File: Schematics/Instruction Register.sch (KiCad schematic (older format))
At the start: 44 parts, among them U46 74F157, U47 74F157, U48 74F574, U49 74F157, U50 74F157, U51 74F574

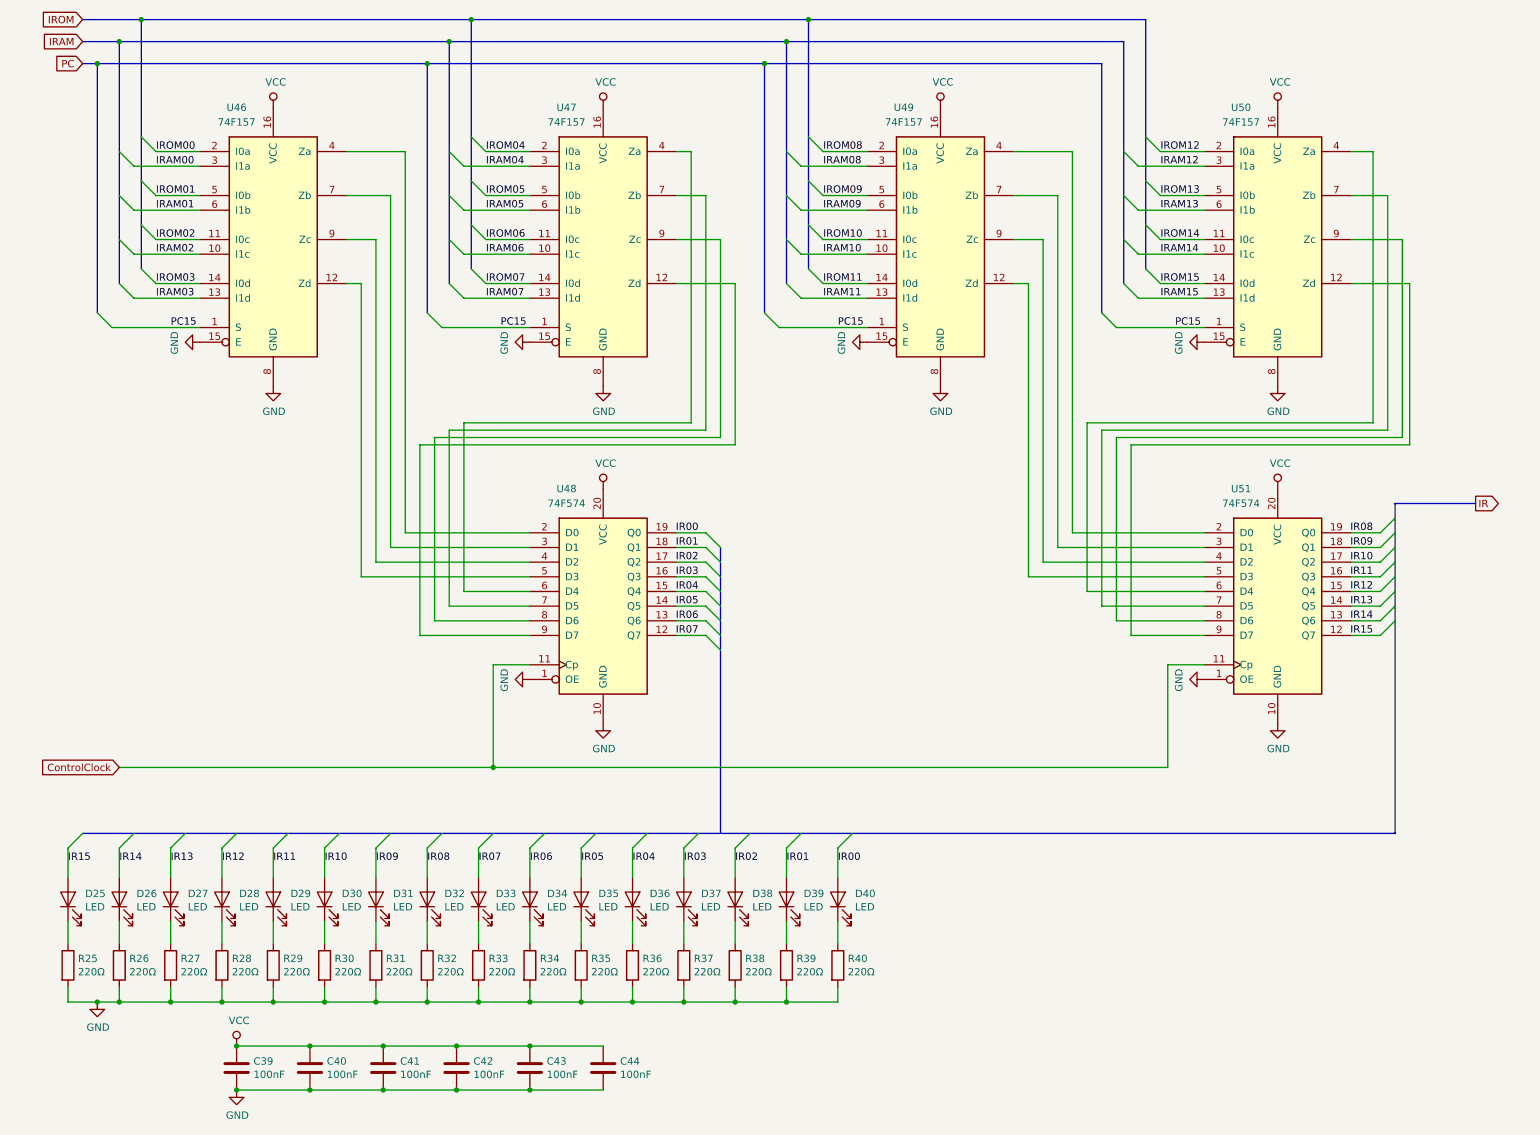
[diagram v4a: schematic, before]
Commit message: My buses were not named according the rules in the Eeschema manual.
Buses which connect to global labels must be named specially.
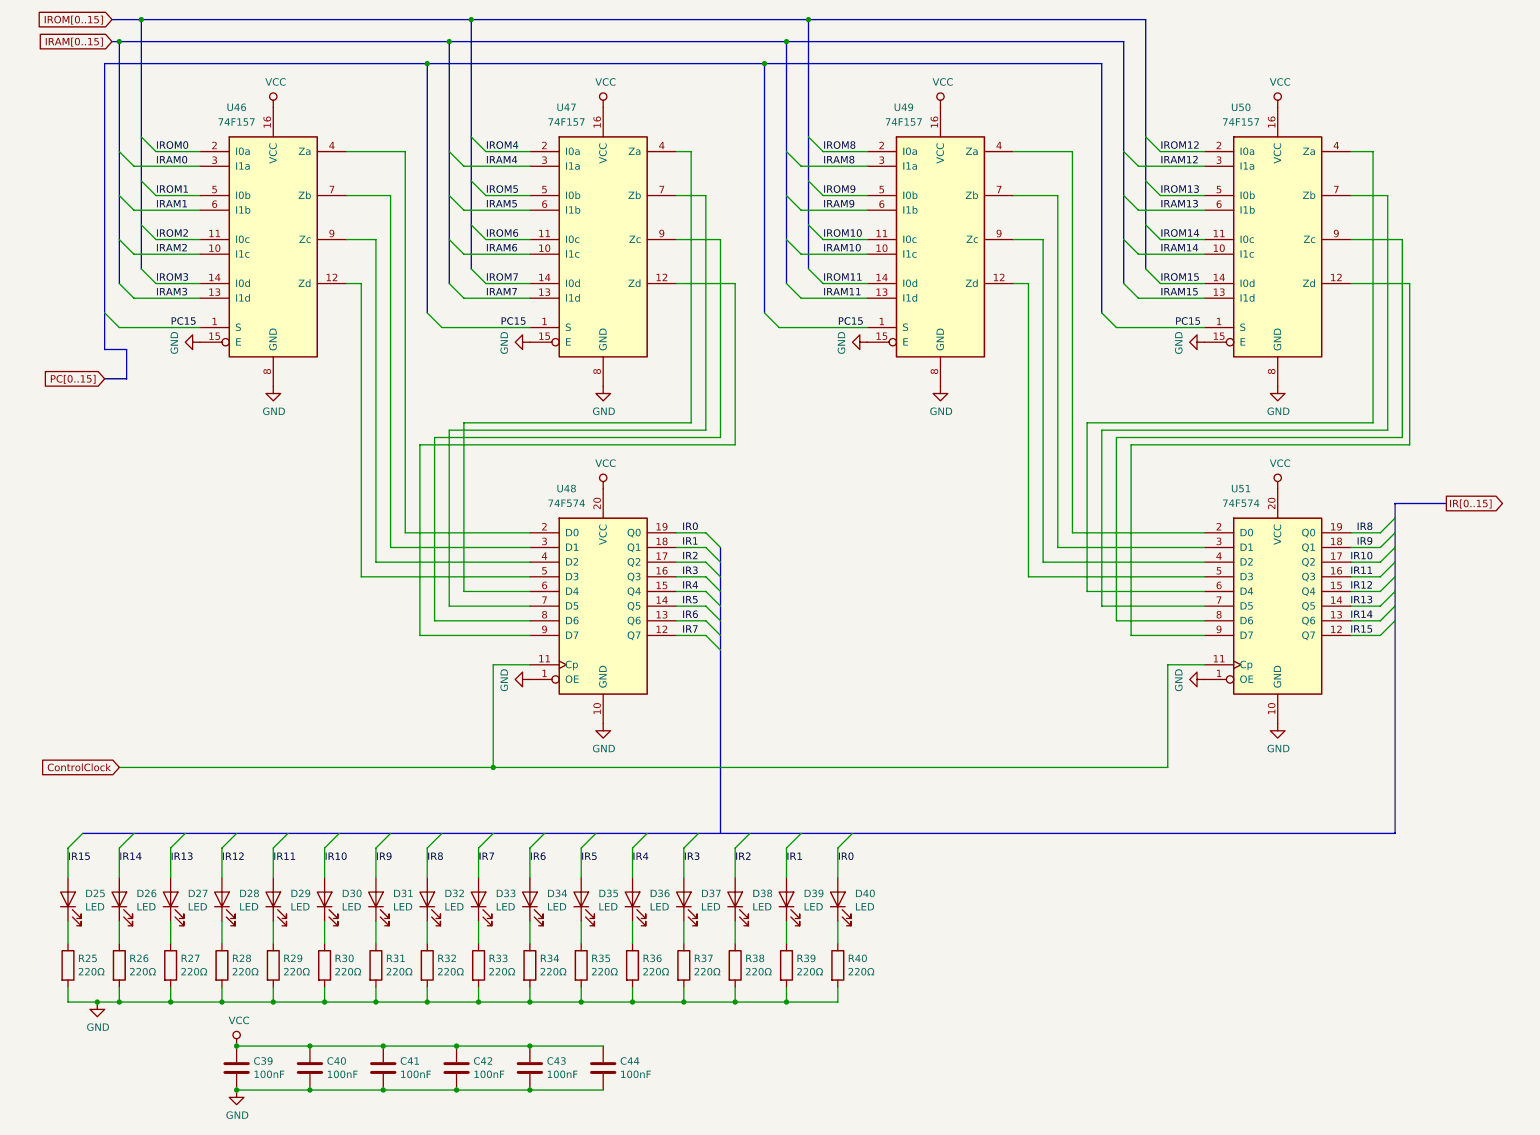
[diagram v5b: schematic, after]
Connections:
- net IR00 renamed IR0
- net IR01 renamed IR1
- net IR02 renamed IR2
- net IR03 renamed IR3
- net IR04 renamed IR4
- net IR05 renamed IR5
- net IR06 renamed IR6
- net IR07 renamed IR7
- net IR08 renamed IR8
- net IR09 renamed IR9
- net IRAM00 renamed IRAM0
- net IRAM01 renamed IRAM1
- net IRAM02 renamed IRAM2
- net IRAM03 renamed IRAM3
- net IRAM04 renamed IRAM4
- net IRAM05 renamed IRAM5
- net IRAM06 renamed IRAM6
- net IRAM07 renamed IRAM7
- net IRAM08 renamed IRAM8
- net IRAM09 renamed IRAM9
- net IROM00 renamed IROM0
- net IROM01 renamed IROM1
- net IROM02 renamed IROM2
- net IROM03 renamed IROM3
- net IROM04 renamed IROM4
- net IROM05 renamed IROM5
- net IROM06 renamed IROM6
- net IROM07 renamed IROM7
- net IROM08 renamed IROM8
- net IROM09 renamed IROM9
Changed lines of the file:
@@
 	9650 4800 9450 4800
 Wire Bus Line
-	9750 3900 10300 3900
+	9750 3900 10100 3900
 Text Label 5000 4100 2    50   ~ 0
-IR00
+IR0
 Text Label 5000 4200 2    50   ~ 0
-IR01
+IR1
 Text Label 5000 4300 2    50   ~ 0
-IR02
+IR2
 Text Label 5000 4400 2    50   ~ 0
-IR03
+IR3
 Text Label 5000 4500 2    50   ~ 0
-IR04
+IR4
 Text Label 5000 4600 2    50   ~ 0
-IR05
+IR5
 Text Label 5000 4700 2    50   ~ 0
-IR06
+IR6
 Text Label 5000 4800 2    50   ~ 0
-IR07
+IR7
 Text Label 9600 4100 2    50   ~ 0
-IR08
+IR8
 Text Label 9600 4200 2    50   ~ 0
-IR09
+IR9
 Text Label 9600 4300 2    50   ~ 0
 IR10
@@
 	1    0    0    -1
 $EndComp
-Text GLabel 10300 3900 2    50   Output ~ 0
-IR
-Text GLabel 800  600  0    50   Input ~ 0
-IROM
-Text GLabel 800  750  0    50   Input ~ 0
-IRAM
+Text GLabel 10100 3900 2    50   Output ~ 0
+IR[0..15]
+Text GLabel 1000 600  0    50   Input ~ 0
+IROM[0..15]
+Text GLabel 1000 750  0    50   Input ~ 0
+IRAM[0..15]
 Entry Wire Line
 	1300 1500 1200 1400
@@
 	1600 1500 1300 1500
 Text Label 1300 1500 0    50   ~ 0
-IROM00
+IROM0
 Text Label 1300 1800 0    50   ~ 0
-IROM01
+IROM1
 Text Label 1300 2100 0    50   ~ 0
-IROM02
+IROM2
 Text Label 1300 2400 0    50   ~ 0
-IROM03
-Wire Bus Line
-	1200 600  800  600
+IROM3
+Wire Bus Line
+	1200 600  1000 600
 Entry Wire Line
 	1050 1500 1150 1600
@@
 	1600 1600 1150 1600
 Text Label 1300 1600 0    50   ~ 0
-IRAM00
+IRAM0
 Text Label 1300 1900 0    50   ~ 0
-IRAM01
+IRAM1
 Text Label 1300 2200 0    50   ~ 0
-IRAM02
+IRAM2
 Text Label 1300 2500 0    50   ~ 0
-IRAM03
-Wire Bus Line
-	800  750  1050 750
+IRAM3
+Wire Bus Line
+	1000 750  1050 750
 $Comp
 L 74xx:74LS157 U?
@@
 	1    0    0    -1
 $EndComp
-Text GLabel 800  900  0    50   Input ~ 0
-PC
-Wire Bus Line
-	800  900  900  900
-Wire Bus Line
-	900  900  900  2600
-Entry Wire Line
-	900  2600 1000 2700
-Wire Wire Line
-	1000 2700 1600 2700
+Text GLabel 950  3050 0    50   Input ~ 0
+PC[0..15]
+Entry Wire Line
+	950  2600 1050 2700
+Wire Wire Line
+	1050 2700 1600 2700
 Text Label 1400 2700 0    50   ~ 0
 PC15
@@
 	3850 1500 3550 1500
 Text Label 3550 1500 0    50   ~ 0
-IROM04
+IROM4
 Text Label 3550 1800 0    50   ~ 0
-IROM05
+IROM5
 Text Label 3550 2100 0    50   ~ 0
-IROM06
+IROM6
 Text Label 3550 2400 0    50   ~ 0
-IROM07
+IROM7
 Entry Wire Line
 	3300 1500 3400 1600
@@
 	3850 1600 3400 1600
 Text Label 3550 1600 0    50   ~ 0
-IRAM04
+IRAM4
 Text Label 3550 1900 0    50   ~ 0
-IRAM05
+IRAM5
 Text Label 3550 2200 0    50   ~ 0
-IRAM06
+IRAM6
 Text Label 3550 2500 0    50   ~ 0
-IRAM07
+IRAM7
 Wire Bus Line
 	3150 900  3150 2600
@@
 Connection ~ 1050 750
 Wire Bus Line
-	3150 900  900  900
-Connection ~ 900  900
+	3150 900  950  900
 Text Label 3650 2700 0    50   ~ 0
 PC15
@@
 	6150 1500 5850 1500
 Text Label 5850 1500 0    50   ~ 0
-IROM08
+IROM8
 Text Label 5850 1800 0    50   ~ 0
-IROM09
+IROM9
 Text Label 5850 2100 0    50   ~ 0
 IROM10
@@
 	6150 1600 5700 1600
 Text Label 5850 1600 0    50   ~ 0
-IRAM08
+IRAM8
 Text Label 5850 1900 0    50   ~ 0
-IRAM09
+IRAM9
 Text Label 5850 2200 0    50   ~ 0
 IRAM10
@@
 	5950 6450 5950 6250
 Text Label 5950 6350 0    50   ~ 0
-IR00
+IR0
 Text Label 5600 6350 0    50   ~ 0
-IR01
+IR1
 Text Label 5250 6350 0    50   ~ 0
-IR02
+IR2
 Text Label 4900 6350 0    50   ~ 0
-IR03
+IR3
 Text Label 4550 6350 0    50   ~ 0
-IR04
+IR4
 Text Label 4200 6350 0    50   ~ 0
-IR05
+IR5
 Text Label 3850 6350 0    50   ~ 0
-IR06
+IR6
 Text Label 3500 6350 0    50   ~ 0
-IR07
+IR7
 Text Label 3150 6350 0    50   ~ 0
-IR08
+IR8
 Text Label 2800 6350 0    50   ~ 0
-IR09
+IR9
 Text Label 2450 6350 0    50   ~ 0
 IR10
@@
 Connection ~ 1850 7900
 Wire Bus Line
+	950  2850 1100 2850
+Wire Bus Line
+	1100 2850 1100 3050
+Wire Bus Line
+	950  3050 1100 3050
+Wire Bus Line
+	950  900  950  2850
+Wire Bus Line
 	7900 750  7900 2400
